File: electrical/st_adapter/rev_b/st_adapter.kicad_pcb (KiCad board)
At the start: 2 copper layers, 40 x 24.6 mm, 2 parts, among them CN1 STADAPTER;M2x4RA, CN2A STLINK;4xF1x2+F1x4+F1x6

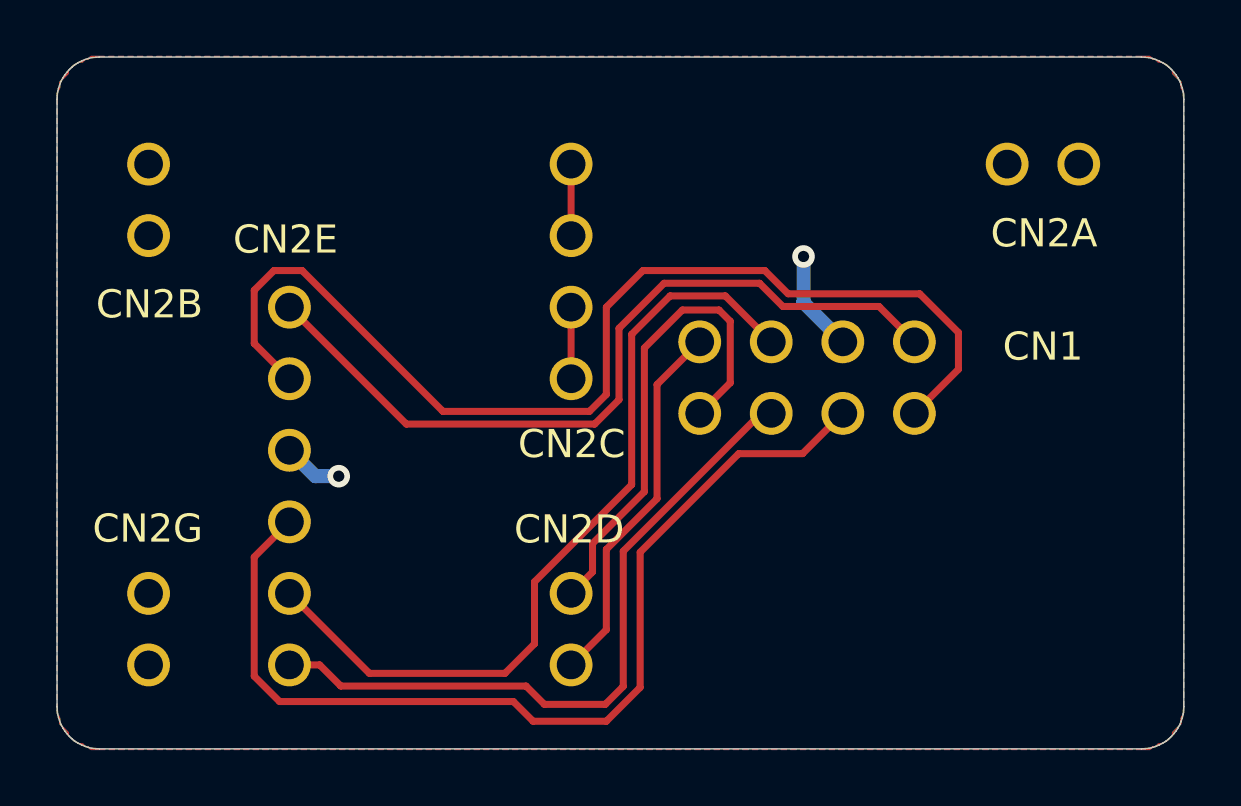
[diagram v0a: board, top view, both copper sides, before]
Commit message: Updated encoder/st-link Rev. B PCB's
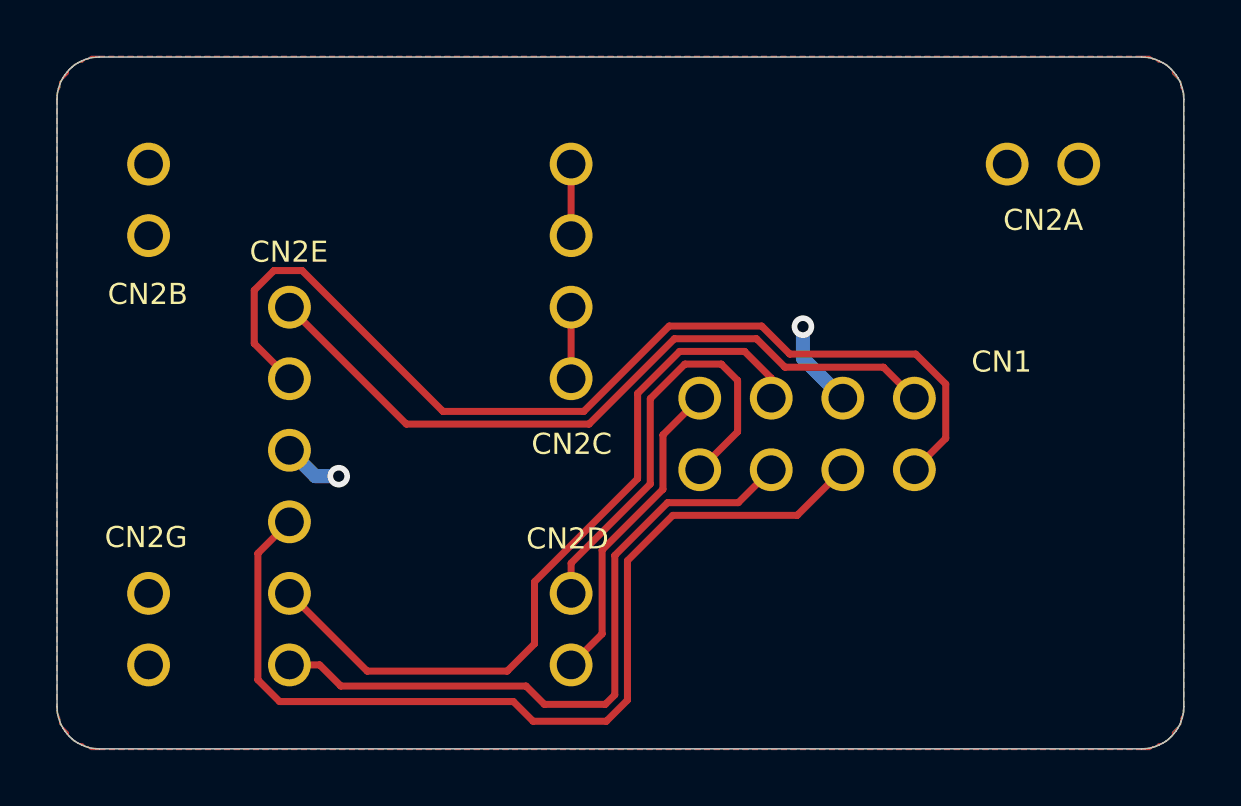
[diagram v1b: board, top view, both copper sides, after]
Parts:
- moved CN1 2.00 mm to (100.0, 102.0)
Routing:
- net /SWCLK: track 39.3 -> 36.2 mm
- net /3V3: track 28.3 -> 26.0 mm
- net /RX: track 13.4 -> 11.4 mm
- net /NRST: track 28.9 -> 27.1 mm
- net /TX: track 17.3 -> 15.7 mm
- net /SWDIO: track 34.9 -> 34.0 mm
- net /SWO: track 24.8 -> 24.0 mm
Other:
- board text added: "HR2 ST ADAPTER License: MIT Date: 2021Jan21 Rev. B Copyright © 2019-21 Homebrew Robotics Club"
- board text removed: "HR2 ST ADAPTER Copyright © 2019-20 Homebrew Robotics Club License: MIT Date: 2020Dec26 Rev. A"
